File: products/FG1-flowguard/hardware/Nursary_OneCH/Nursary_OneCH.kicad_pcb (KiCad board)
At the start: 2 copper layers, 29.8 x 94.8 mm, 38 parts, among them J1 FLOW1_CONN, J2 Relay1_CONN, J3 PWR_CONN, J4 FLOW2_CONN, K1 Cube_Relay, U1 ULN2003, U3 DS1307Z+, U4 DS3231M, U5 ESP32 30 Pin CP2102 Developme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, Y1 Crystal

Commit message: Update Nursary_OneCH hardware
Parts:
- removed ., H1: MountingHole, MountingHole:MountingHole_3.2mm_M3
- removed C3: 200pF, Capacitor_SMD:C_0805_2012Metric
- removed C5: 100nF, Capacitor_SMD:C_0805_2012Metric
- removed D2, D5: PESD3V3U1UL, Diode_SMD:D_SOD-882
- removed D3: LED_GREEN_FLOW, LED_SMD:LED_0603_1608Metric
- removed F2: Polyfuse_Small, Inductor_SMD:L_1206_3216Metric
- removed J3: PWR_CONN, Connector_PinHeader_2.00mm:PinHeader_1x02_P2.00mm_Vertical
- removed J3: PWR_CONN, Connector_JST:JST_EH_B2B-EH-A_1x02_P2.50mm_Vertical
- removed R2, R6: 100E, Resistor_SMD:R_0805_2012Metric
- removed R7: 10K, Resistor_SMD:R_0805_2012Metric
- removed R8: 470E, Resistor_SMD:R_0805_2012Metric
- removed R9: 2K2, Resistor_SMD:R_0805_2012Metric
- added ?: , , F.Cu at (220.8, 47.7)
- added ?: , , F.Cu at (220.8, 131.7)
- added ?: , , F.Cu at (190.8, 131.7)
- added ?: , , F.Cu at (190.8, 47.7)
- added D6: PESD3V3U1UL, Diode_SMD:D_SOD-882, B.Cu at (185.9, 100.1)
- C2: value 200pF -> 100pF
- D1, D4: footprint LED_SMD:LED_0603_1608Metric -> LED_SMD:LED_0805_2012Metric
- J1: value FLOW1_CONN -> Conn_IN; footprint Connector_JST:JST_EH_B3B-EH-A_1x03_P2.50mm_Vertical -> Connector_Phoenix_MSTB:PhoenixContact_MSTBVA_2,5_3-G-5,08_1x03_P5.08mm_Vertical
- J2: footprint Connector_JST:JST_EH_B2B-EH-A_1x02_P2.50mm_Vertical -> Connector_Phoenix_MSTB:PhoenixContact_MSTBVA_2,5_2-G-5,08_1x02_P5.08mm_Vertical
- J4: value FLOW2_CONN -> Conn_01x02_Pin; footprint Connector_JST:JST_EH_B3B-EH-A_1x03_P2.50mm_Vertical -> Connector_JST:JST_PH_B2B-PH-K_1x02_P2.00mm_Vertical
- R1: value 2K2 -> 470E
- U1: footprint Package_SO:SOIC-16W_5.3x10.2mm_P1.27mm -> Package_SO:SOIC-16_3.9x9.9mm_P1.27mm
- moved J2 128.6 mm to (223.3, 119.0)
- moved U1 113.1 mm to (224.2, 81.0), turned to -90 degrees
- moved D4 106.2 mm to (223.8, 59.0), turned to -90 degrees
- moved C6 105.3 mm to (229.7, 89.8), turned to 90 degrees
- moved R5 103.5 mm to (223.9, 63.4), turned to 90 degrees
- moved C4 102.1 mm to (224.6, 88.8), turned to 90 degrees
- moved K1 98.9 mm to (224.2, 93.9), turned to -90 degrees
- moved C2 86.8 mm to (196.2, 69.6)
- moved D1 86.5 mm to (179.3, 59.0), turned to -90 degrees
- moved U4 85.6 mm to (206.7, 123.4)
- moved R3 84.0 mm to (179.2, 63.5)
- moved Y1 83.9 mm to (198.2, 117.9)
- moved BT1 83.5 mm to (203.2, 132.0)
- moved R4 82.3 mm to (196.3, 75.7)
- moved U5 82.2 mm to (213.4, 95.0)
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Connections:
- net /FLOW1_CONN renamed /FLOW1_CON
- C2 pad 1: /FLOW1_PROT -> /FLOW1_MCU
- C4 pad 1: +5VR -> +5V
- C6 pad 1: +5VR -> +5V
- D1 pad 1: /FLOW1_PROT -> GND
- J4 pad 1: +5VP -> GND
- J4 pad 2: /FLOW2_CONN -> +5V
- K1 pad 5: +5VR -> +5V
- R1 pad 1: /FLOW1_PROT -> /FLOW1_MCU
- R3 pad 1: +5VP -> /FLOW1_LED_MCU
- R4 pad 2: /FLOW1_PROT -> /FLOW1_MCU
- R5 pad 1: +5VR -> +5V
- U1 pad 9: +5VR -> +5V
- U5 pad 19: /FLOW2_MCU -> unconnected-(U5-D34/Input_only-Pad19)
- U5 pad 21: unconnected-(U5-D32-Pad21) -> /FLOW1_LED_MCU
- Y1 pad 1: Net-(U3-X1) -> Net-(U3-X2)
- Y1 pad 2: Net-(U3-X2) -> Net-(U3-X1)
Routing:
- net /FLOW1_PROT: track 61.7 -> 0.00 mm, vias 1 -> 0
- net /FLOW2_PROT: track 59.4 -> 0.00 mm, vias 3 -> 0
- net /SCL: track 56.0 -> 88.9 mm, vias 0 -> 2
- net /FLOW1_MCU: track 2.74 -> 33.9 mm
- net /SDA: track 47.5 -> 77.7 mm, vias 0 -> 2
- net /RELAY1_MCU: track 40.5 -> 11.8 mm, vias 2 -> 0
- net +5VR: track 28.5 -> 0.00 mm
- net +5V: track 115.8 -> 141.7 mm, vias 1 -> 0
- net +5VP: track 28.7 -> 12.0 mm
- net /FLOW1_LED_MCU: track 0.00 -> 16.0 mm
- net /FLOW1_CON: track 4.99 -> 15.4 mm
- net Net-(J2-Pin_2): track 26.2 -> 35.8 mm
- net /BATT: track 39.5 -> 46.5 mm, vias 2 -> 0
- net GND: track 5.72 -> 0.00 mm, vias 75 -> 45
- net Net-(D3-A): track 5.46 -> 0.00 mm, vias 3 -> 0
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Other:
- board size 29.8 x 94.8 mm -> 57.1 x 91.8 mm
- board text added: "Agri Sensors and Controls Aug2026"
- board text added: "FLOW"
- board text added: "GND"
- board text added: "RLY"
- board text added: "SIG"
- board text added: "Y"
- board text removed: "+BATT"
- board text removed: "Agri Sensors and Controls Jul2026"
- board text removed: "FL1"
- board text removed: "FL2"
- board text removed: "Pump OUT"

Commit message: Update Nursary_OneCH hardware
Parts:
- added TP1: TestPoint, TestPoint:TestPoint_Keystone_5019_Miniature, B.Cu at (196.9, 124.2)
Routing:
- net /BATT: track 46.5 -> 47.4 mm
- net GND: vias 45 -> 51

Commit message: Update Nursary_OneCH hardware
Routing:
- net +5V: track 141.7 -> 144.3 mm
- net GND: vias 51 -> 84

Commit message: hardware: KiCad/Gerber updates for Nursary_OneCH (V3 export)
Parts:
- moved R3 1.52 mm to (179.2, 65.0)
- moved R5 1.41 mm to (223.9, 64.8)
- moved D6 0.05 mm to (186.0, 100.1)
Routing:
- net /FLOW1_LED_MCU: track 16.0 -> 14.5 mm
- net +5V: track 144.3 -> 142.9 mm

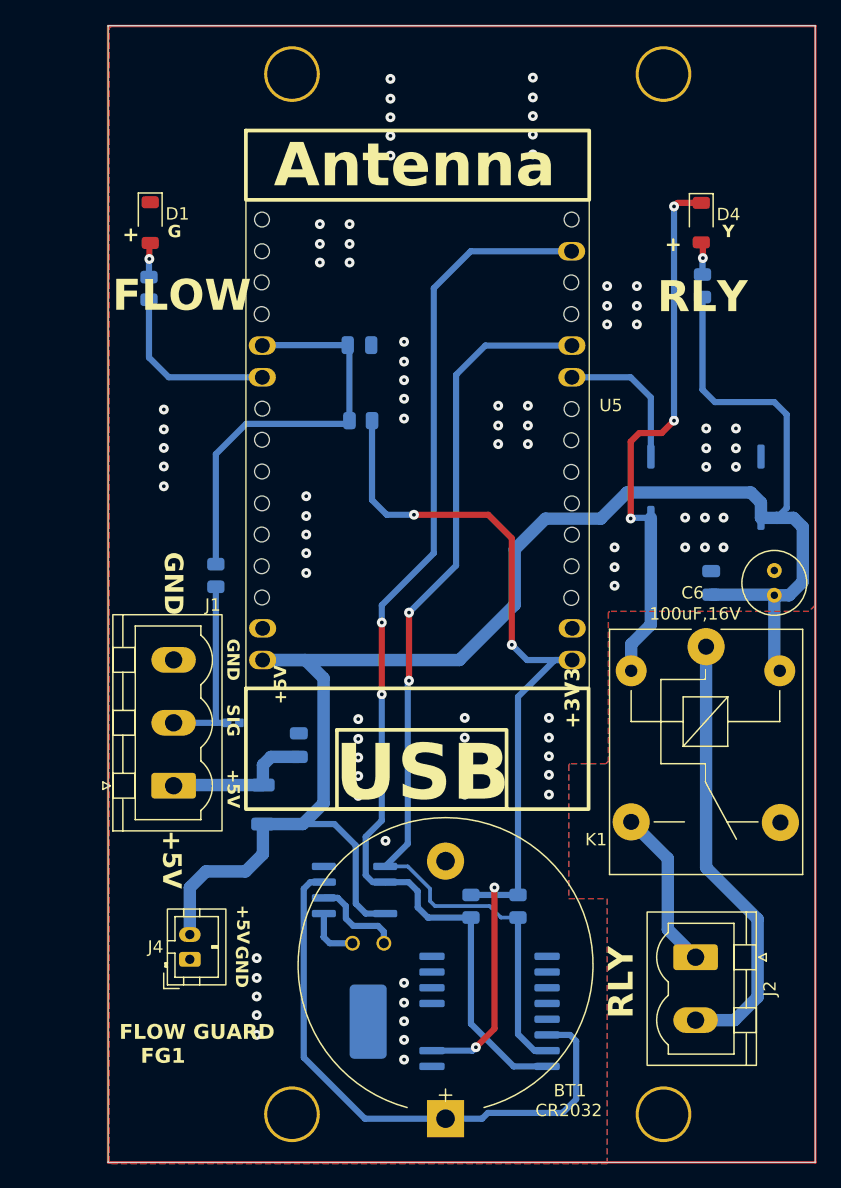
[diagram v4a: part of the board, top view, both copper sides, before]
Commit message: feat: missed-cycle catch-up + PCB connector adjustment + test automation spec
Scheduler: a cycle whose scheduled start fell entirely within a power
outage (device down before AND after the trigger minute) was
previously skipped for the day with no catch-up -- checkPowerRecovery()
only resumes an already-running cycle, and the exact-minute trigger has
no memory of a missed minute. Added missed-cycle catch-up: on boot, any
enabled cycle whose start time has already passed today and hasn't run
since that scheduled time gets started now, for its full configured
duration/target, same as an on-time start.

Fixed two interaction bugs found while testing this on real hardware:
(1) catching up during begin() raced ahead of checkPowerRecovery(),
so a genuinely mid-run cycle interrupted by a second outage got
restarted from zero instead of resumed -- reordered so resume always
gets first refusal, with defensive guards on both sides; (2) the
catch-up check was keyed on any history entry for this cycle today,
so a cycle rescheduled to a new time after already running once earlier
the same day was wrongly skipped -- now anchored on history since the
cycle's CURRENT scheduled time specifically. Also restored an immediate
schedule check right after boot recovery, using the RTC's own time,
instead of waiting on the full WiFi/NTP/MQTT sequence to complete --
matters most exactly when it's needed most, since a power outage often
takes the router down too.

Hardware: adjusted connector position on Nursary_OneCH PCB (gerbers +
KiCad project regenerated) -- Avinash to test fit on his unit.

Added FG1 test jig specification (docs/testing/TEST_JIG_SPEC.md) and
a working Python test automation harness (products/FG1-flowguard/testing/)
-- flash + boot-log verification is usable today; production/full test
tiers are written against the jig's serial protocol, ready to wire up
once the physical jig exists.
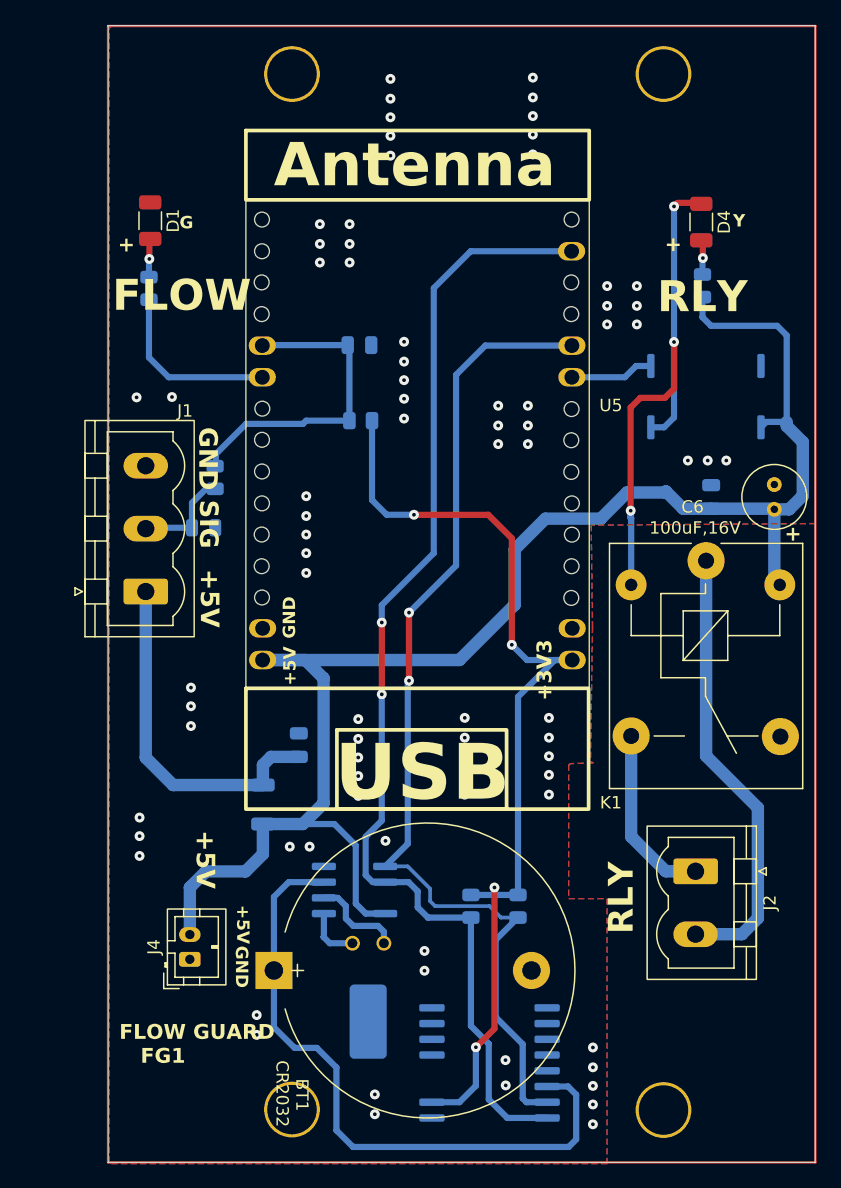
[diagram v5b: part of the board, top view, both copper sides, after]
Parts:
- D1, D4: footprint LED_SMD:LED_0805_2012Metric -> Capacitor_SMD:C_1206_3216Metric
- D6: value PESD3V3U1UL -> PESD; footprint Diode_SMD:D_SOD-882 -> Diode_SMD:D_0805_2012Metric
- moved BT1 18.3 mm to (189.3, 120.1), turned to 0 degrees
- moved D6 15.9 mm to (183.6, 84.3)
- moved J1 15.8 mm to (178.9, 89.5)
- moved R1 7.91 mm to (184.5, 80.3)
- moved U1 7.31 mm to (224.2, 73.7)
- moved C4 6.94 mm to (224.6, 81.8)
- moved C6 6.94 mm to (229.7, 82.8)
- moved J2 6.94 mm to (223.3, 112.1)
- moved K1 6.94 mm to (224.2, 87.0)
- moved U4 4.16 mm to (206.7, 127.5)
- moved D4 0.61 mm to (223.8, 59.6)
- moved D1 0.55 mm to (179.3, 59.5)
- moved ? 0.38 mm to (190.8, 131.3)
- moved ? 0.34 mm to (220.8, 131.3)
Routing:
- net +5VP: track 12.0 -> 28.6 mm
- net +5V: track 142.9 -> 130.9 mm
- net /FLOW1_MCU: track 33.9 -> 26.0 mm
- net /FLOW1_CON: track 15.4 -> 8.20 mm
- net /BATT: track 47.4 -> 54.0 mm
- net /SDA: track 77.7 -> 83.8 mm
- net /RELAY1_MCU: track 11.8 -> 6.75 mm
- net /SCL: track 88.9 -> 93.4 mm
- net +3.3V: track 76.2 -> 79.7 mm
- net Net-(J2-Pin_1): track 13.1 -> 14.5 mm
- net GND: vias 84 -> 80
